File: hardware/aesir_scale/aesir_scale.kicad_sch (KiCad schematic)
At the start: 44 parts, among them J1 jst xh 4, J2 jst gh, J3 jst xh 4, J5 jst gh, J8 USB_C_Receptacle_USB2.0, J9 jst_sh 6, U1 STM32U575CGTx, U2 NAU7802SGI, U3 AZ1117CH2-3.3TRG1, U4 TJA1051T, Y1 48MHz

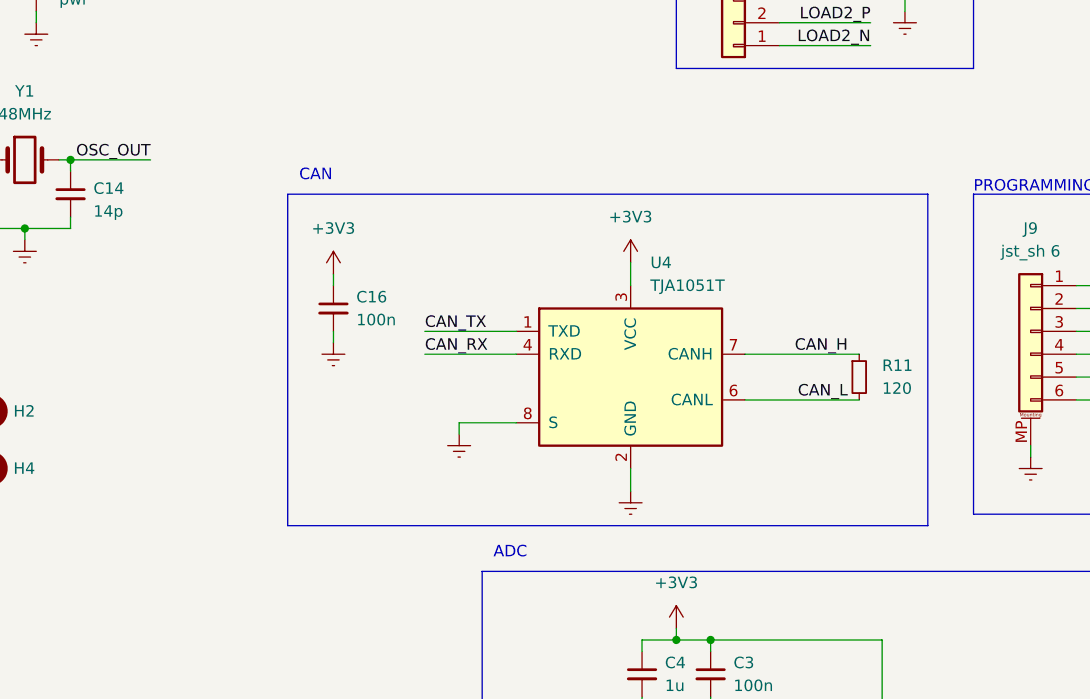
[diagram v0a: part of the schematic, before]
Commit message: USB diode & CAN jumper
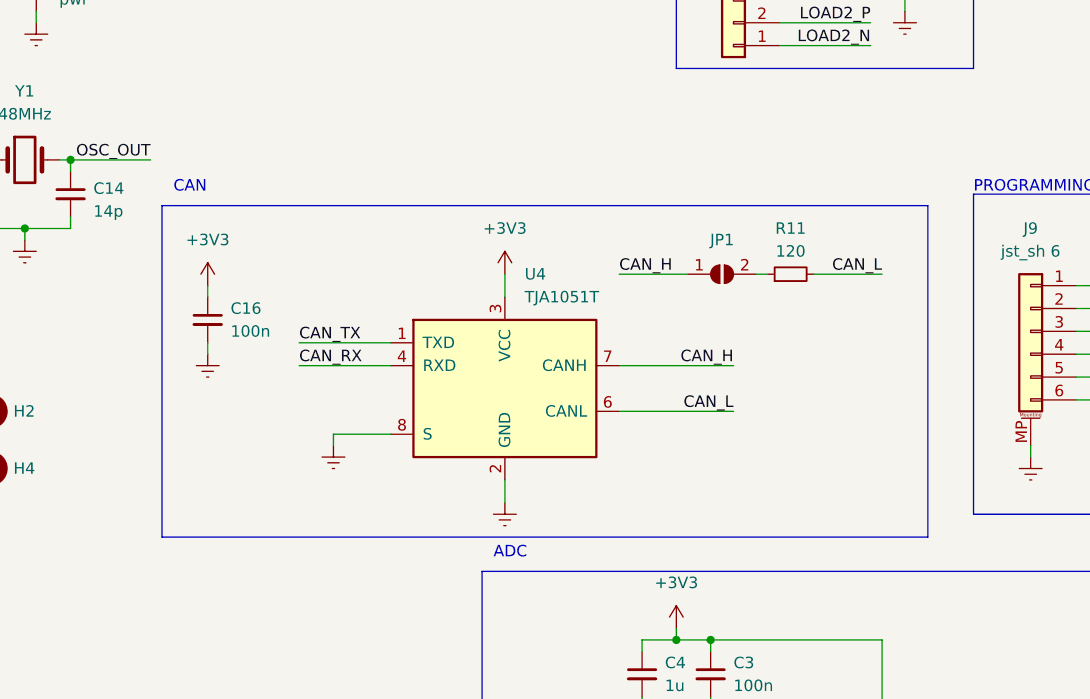
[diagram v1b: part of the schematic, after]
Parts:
- added JP1: SolderJumper_2_Open, Jumper:SolderJumper-2_P1.3mm_Open_TrianglePad1.0x1.5mm, symbol Jumper:SolderJumper_2_Open
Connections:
- net CAN_H: now also JP1.1 (A); no longer R11.1
- new net: JP1.2 (B), R11.1
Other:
- moved on the sheet: C16, R11, U4

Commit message: add caps
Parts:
- added C8: 4u7, Capacitor_SMD:C_0603_1608Metric_Pad1.08x0.95mm_HandSolder, symbol Device:C_Small
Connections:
- net +3V3: now also C8.1
- net Earth: now also C8.2
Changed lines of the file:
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@@
   (junction (at 111.76 76.2) (diameter 0) (color 0 0 0 0)
   )
+  (junction (at 97.79 20.32) (diameter 0) (color 0 0 0 0)
+  )
   (junction (at 184.15 149.86) (diameter 0) (color 0 0 0 0)
   )
@@
   )
   (junction (at 184.15 121.92) (diameter 0) (color 0 0 0 0)
+  )
+  (junction (at 97.79 27.94) (diameter 0) (color 0 0 0 0)
   )
   (junction (at 65.405 152.4) (diameter 0) (color 0 0 0 0)
@@
     (stroke (width 0) (type default))
   )
+  (wire (pts (xy 107.95 27.94) (xy 107.95 26.67))
+    (stroke (width 0) (type default))
+  )
   (wire (pts (xy 66.04 26.67) (xy 64.77 26.67))
     (stroke (width 0) (type default))
@@
     (stroke (width 0) (type default))
   )
+  (wire (pts (xy 107.95 21.59) (xy 107.95 20.32))
+    (stroke (width 0) (type default))
+  )
   (wire (pts (xy 259.08 106.68) (xy 259.08 107.95))
     (stroke (width 0) (type default))
@@
     (stroke (width 0) (type default))
   )
+  (wire (pts (xy 97.79 27.94) (xy 107.95 27.94))
+    (stroke (width 0) (type default))
+  )
   (wire (pts (xy 35.56 185.42) (xy 39.37 185.42))
     (stroke (width 0) (type default))
@@
   )
   (wire (pts (xy 80.01 69.85) (xy 92.71 69.85))
+    (stroke (width 0) (type default))
+  )
+  (wire (pts (xy 97.79 20.32) (xy 107.95 20.32))
     (stroke (width 0) (type default))
   )
@@
         )
       )
+    )
+  )
+  (symbol (lib_id "Device:C_Small") (at 107.95 24.13 0) (unit 1)
+    (in_bom yes) (on_board yes) (dnp no) (fields_autoplaced)
+    (property "Reference" "C8" (at 110.49 22.8663 0)
+      (effects (font (size 1.27 1.27)) (justify left))
+    )
+    (property "Value" "4u7" (at 110.49 25.4063 0)
+      (effects (font (size 1.27 1.27)) (justify left))
+    )
+    (property "Footprint" "Capacitor_SMD:C_0603_1608Metric_Pad1.08x0.95mm_HandSolder" (at 107.95 24.13 0)
+      (effects (font (size 1.27 1.27)) hide)
+    )
+    (property "Datasheet" "~" (at 107.95 24.13 0)
+      (effects (font (size 1.27 1.27)) hide)
+    )
+    (pin "1")
+    (pin "2")
+    (instances
+      (project "aesir_scale"
+        (path "/82095f51-1dde-4058-bc4d-39ef8853952f"
+          (reference "C8") (unit 1)
+        )
+      )

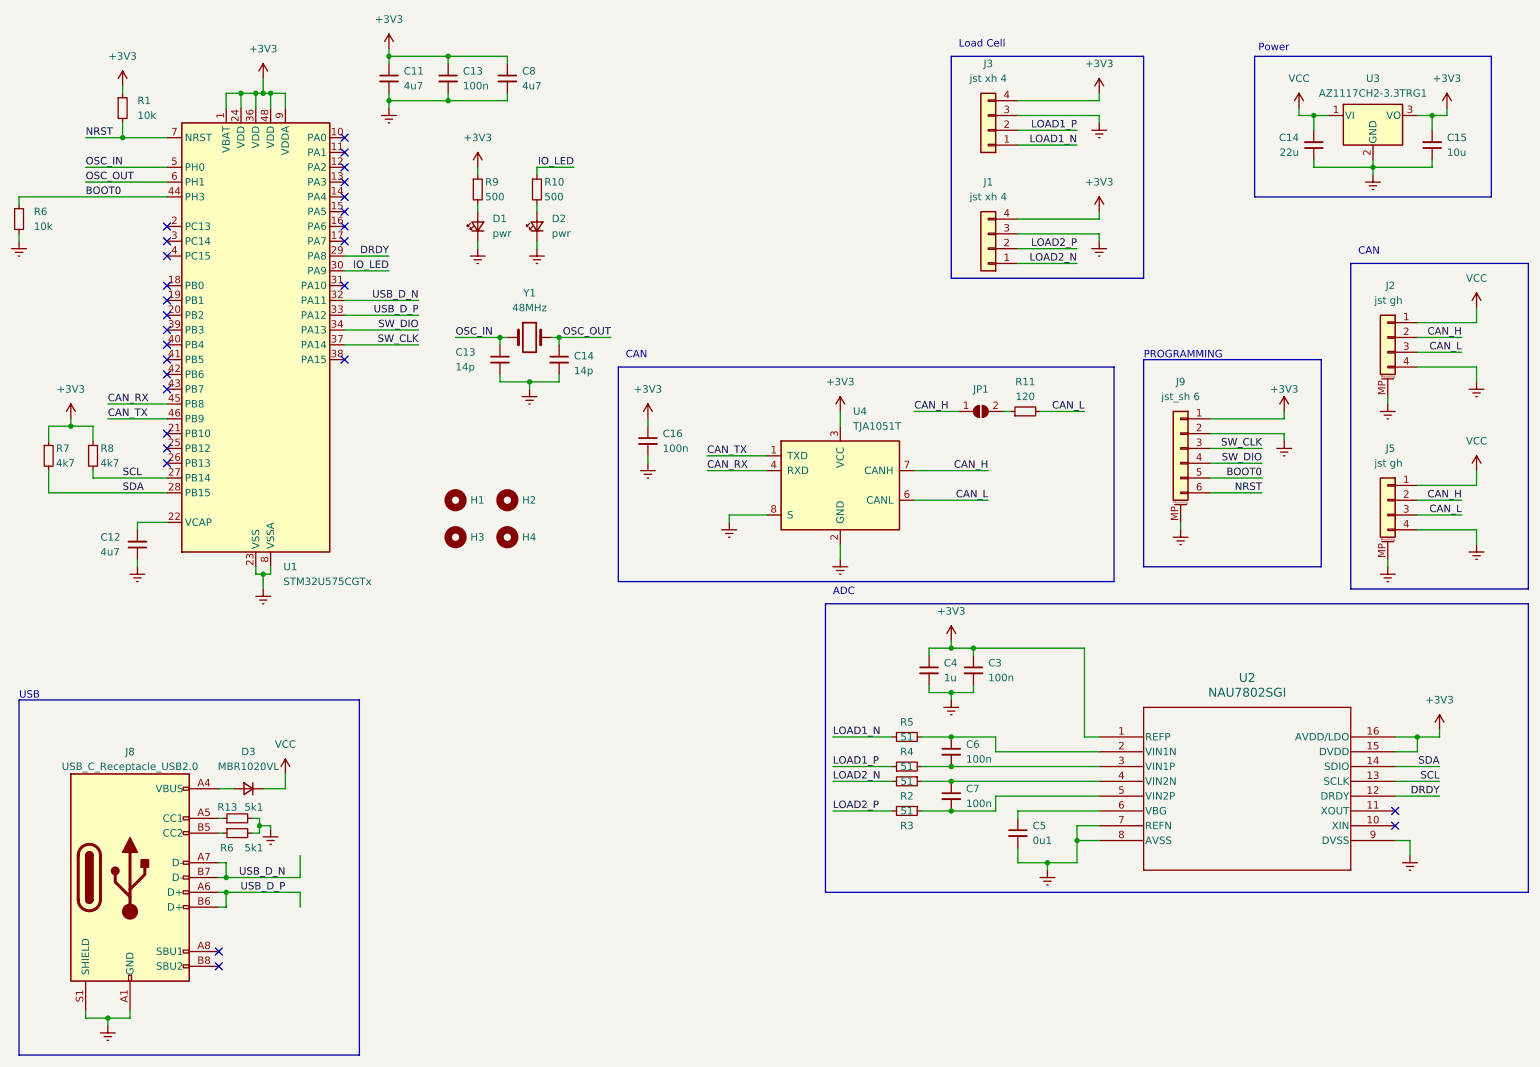
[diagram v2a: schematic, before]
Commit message: correct i2c bus
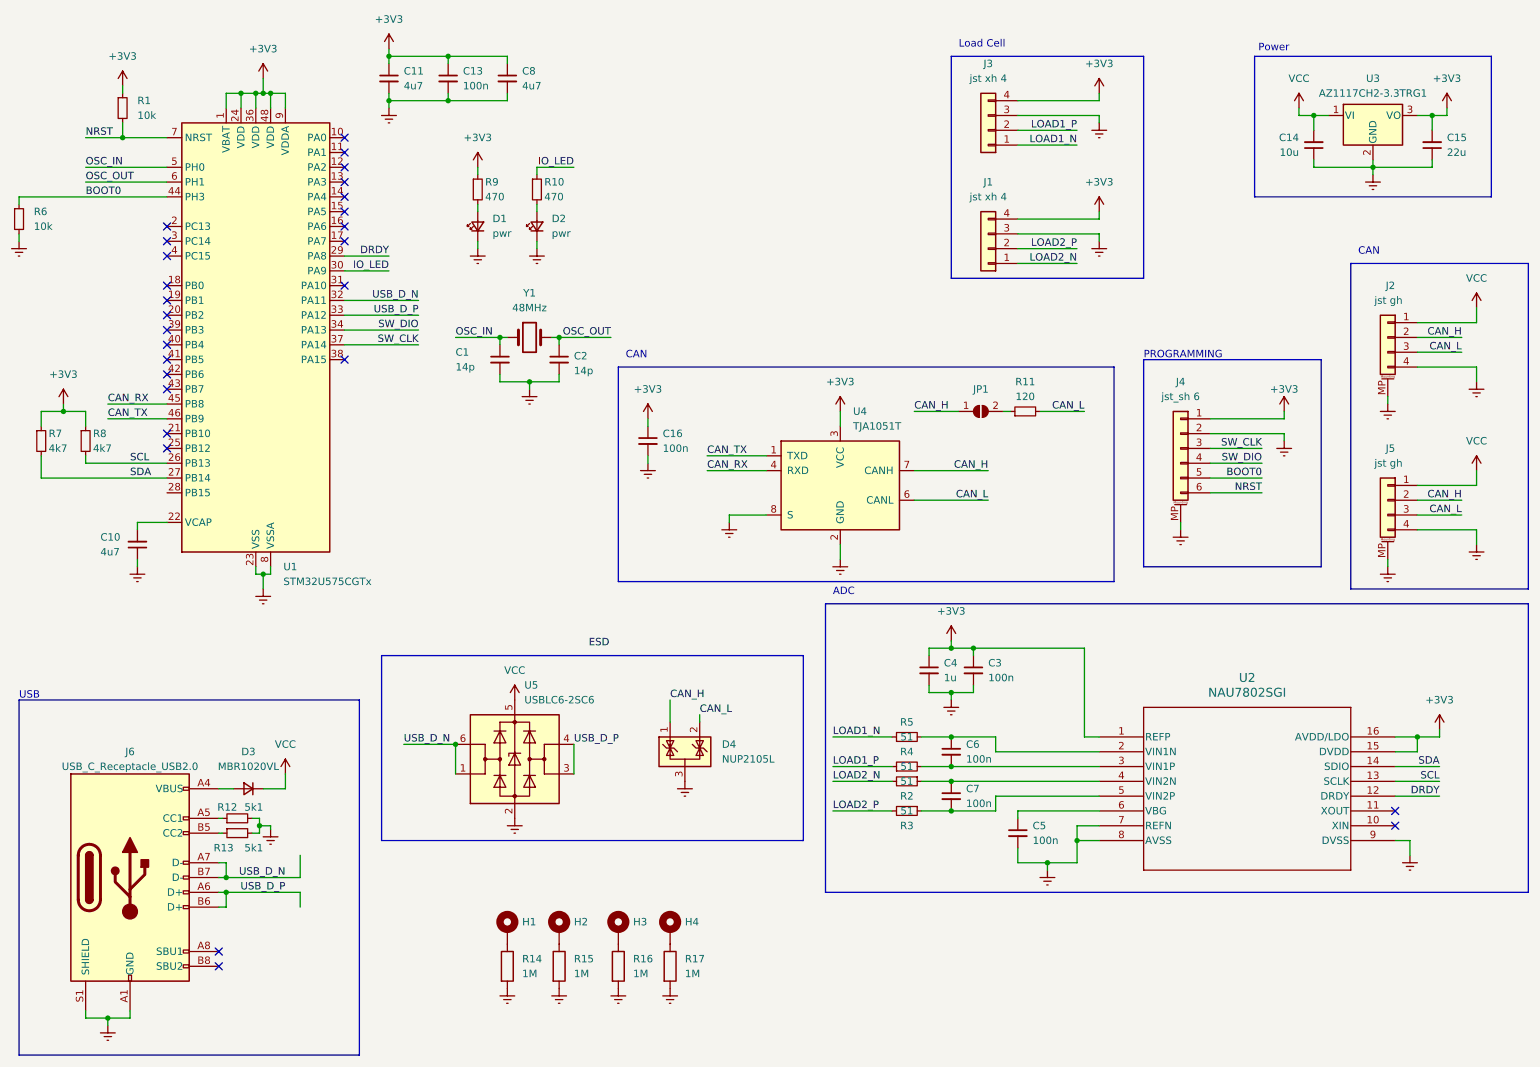
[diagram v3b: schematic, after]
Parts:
- added D4: NUP2105L, Package_TO_SOT_SMD:SOT-23, symbol Power_Protection:NUP2105L
- added R14, R15, R16, R17: 1M, Resistor_SMD:R_0603_1608Metric_Pad0.98x0.95mm_HandSolder, symbol Device:R
- added U5: USBLC6-2SC6, Package_TO_SOT_SMD:SOT-23-6, symbol Power_Protection:USBLC6-2SC6
- C14: value 22u -> 10u
- C15: value 10u -> 22u
- C5: value 0u1 -> 100n
- H1, H2, H3, H4: footprint MountingHole:MountingHole_3.2mm_M3_ISO7380 -> MountingHole:MountingHole_3.2mm_M3_ISO7380_Pad; symbol Mechanical:MountingHole -> Mechanical:MountingHole_Pad
- R10, R9: value 500 -> 470
- renumbered C13 to C1, C12 to C10, C14 to C2, J9 to J4, J8 to J6, R13 to R12, R6 to R13
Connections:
- net CAN_H: now also D4.1 (K)
- net CAN_L: now also D4.2 (K)
- net Earth: now also D4.3 (A), R14.2, R15.2, R16.2, R17.2, U5.2 (GND)
- net SCL: now also U1.26 (PB13); no longer U1.27 (PB14)
- net SDA: now also U1.27 (PB14); no longer U1.28 (PB15)
- net USB_D_N: now also U5.1 (I/O1), U5.6 (I/O1)
- net USB_D_P: now also U5.3 (I/O2), U5.4 (I/O2)
- net VCC: now also U5.5 (VBUS)
- new net: H1.1, R14.1
- new net: H3.1, R16.1
- new net: H4.1, R17.1
- new net: H2.1, R15.1
- no-connect marks 28 -> 27
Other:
- moved on the sheet: R7, R8
